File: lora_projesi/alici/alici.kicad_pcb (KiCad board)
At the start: 4 copper layers, 88 x 102 mm, 127 parts, among them J1 USB-C, J2 SMA, J3 RJ45, J4 u.FL (ANA ANTEN), J5 12 V GIRIS, J6 LAMBA, J7 MICRO-SIM, J8 u.FL (YARDIMCI ANTEN, ISTEGE 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, K1 SRD-12VDC-SL-A, Q1 AO3401A, Q2 MMBT2222A, Q3 MMBT2222A, Q4 MMBT2222A, SW1 DUGME, U1 ESP32-S3-WROOM-1-N4, U10 SIM7600SA, U11 AP2112K-3.3, U12 ESDA6V1-5SC6, U4 RFM95W-915S2, U5 TPS62933DRLR, U6 TPS62933DRLR, U7 USBLC6-2SC6, U8 TXB0104PW, U9 W5500, Y1 25 MHz

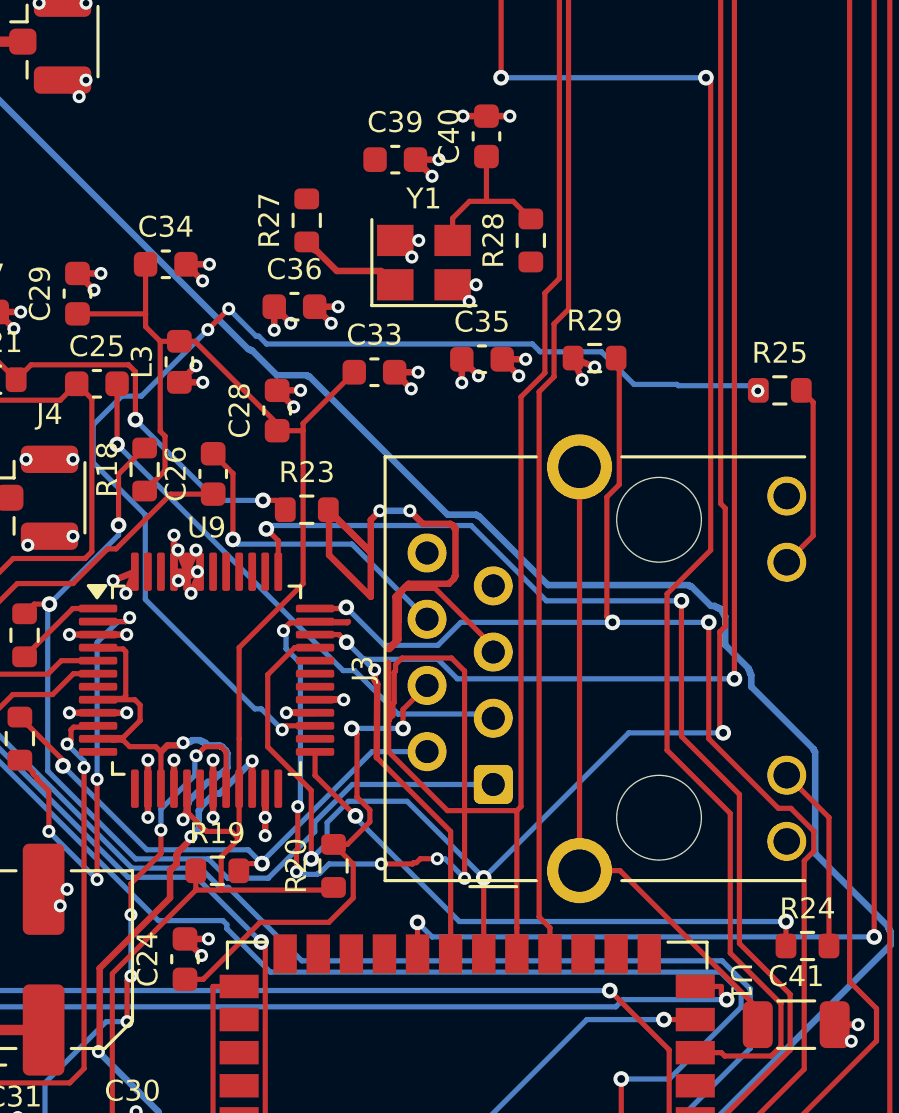
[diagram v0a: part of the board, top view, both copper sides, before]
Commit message: izgara: uc katman (F, B, In2) yonlendirme
Co-Authored-By: Claude Sonnet 5.5 <noreply@anthropic.com>
Claude-Session: https://claude.ai/code/session_01Q71gHQtKJ86ZE2CtYTYSwP
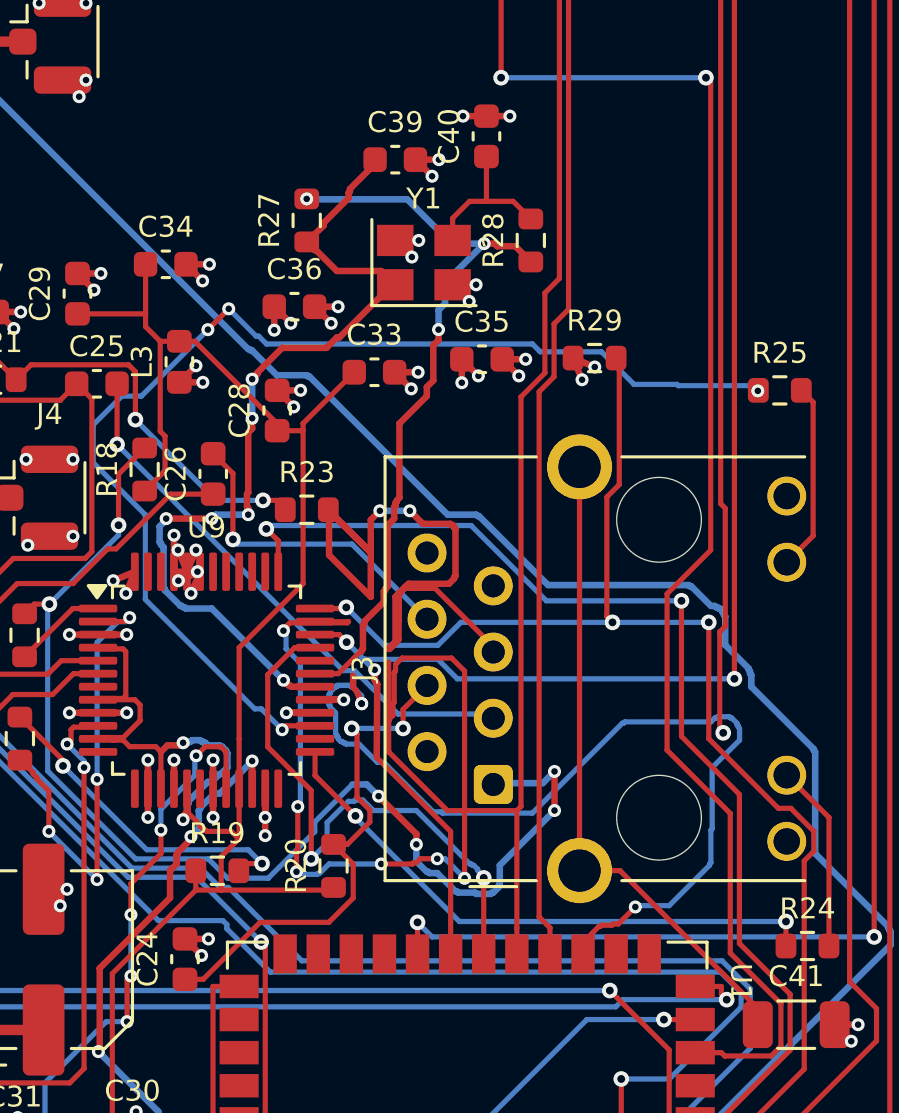
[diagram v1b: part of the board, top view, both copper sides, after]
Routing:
- net ETH_CS: track 0.00 -> 38.3 mm, vias 0 -> 3
- net XI: track 4.08 -> 34.1 mm, vias 0 -> 6
- net XO: track 0.00 -> 29.3 mm, vias 0 -> 3
- net SPI_SCK: track 81.8 -> 70.4 mm, vias 3 -> 4
- net TD_P: track 35.5 -> 46.1 mm, vias 2 -> 7
- net TD_N: track 20.9 -> 12.8 mm

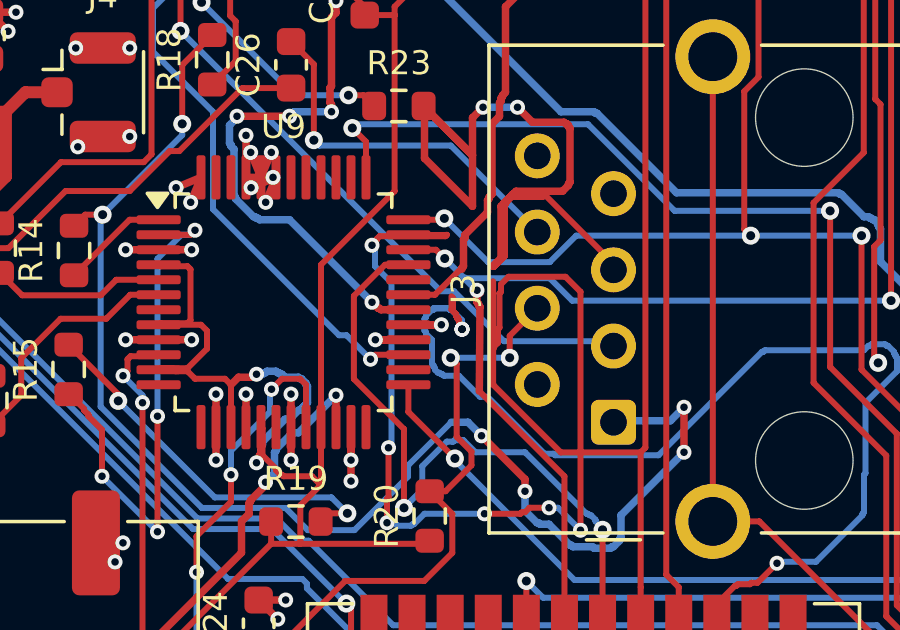
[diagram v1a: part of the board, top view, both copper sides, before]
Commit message: Alici: kristal arka yuz, plane via ic tarafa, boru hatti yeniden
Co-Authored-By: Claude Sonnet 5.5 <noreply@anthropic.com>
Claude-Session: https://claude.ai/code/session_01Q71gHQtKJ86ZE2CtYTYSwP
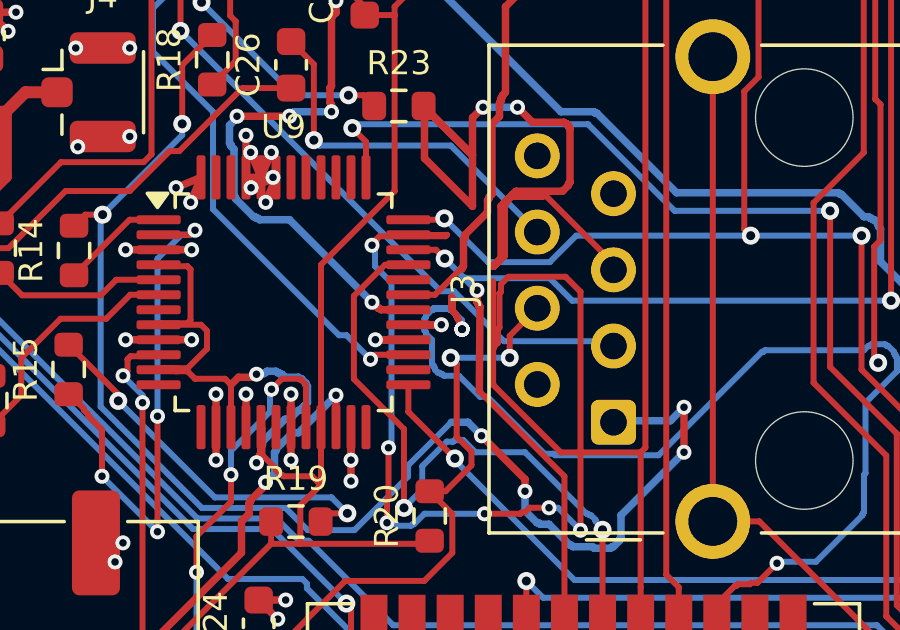
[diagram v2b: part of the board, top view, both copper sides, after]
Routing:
- net ETH_CS: track 38.3 -> 43.6 mm, vias 3 -> 5

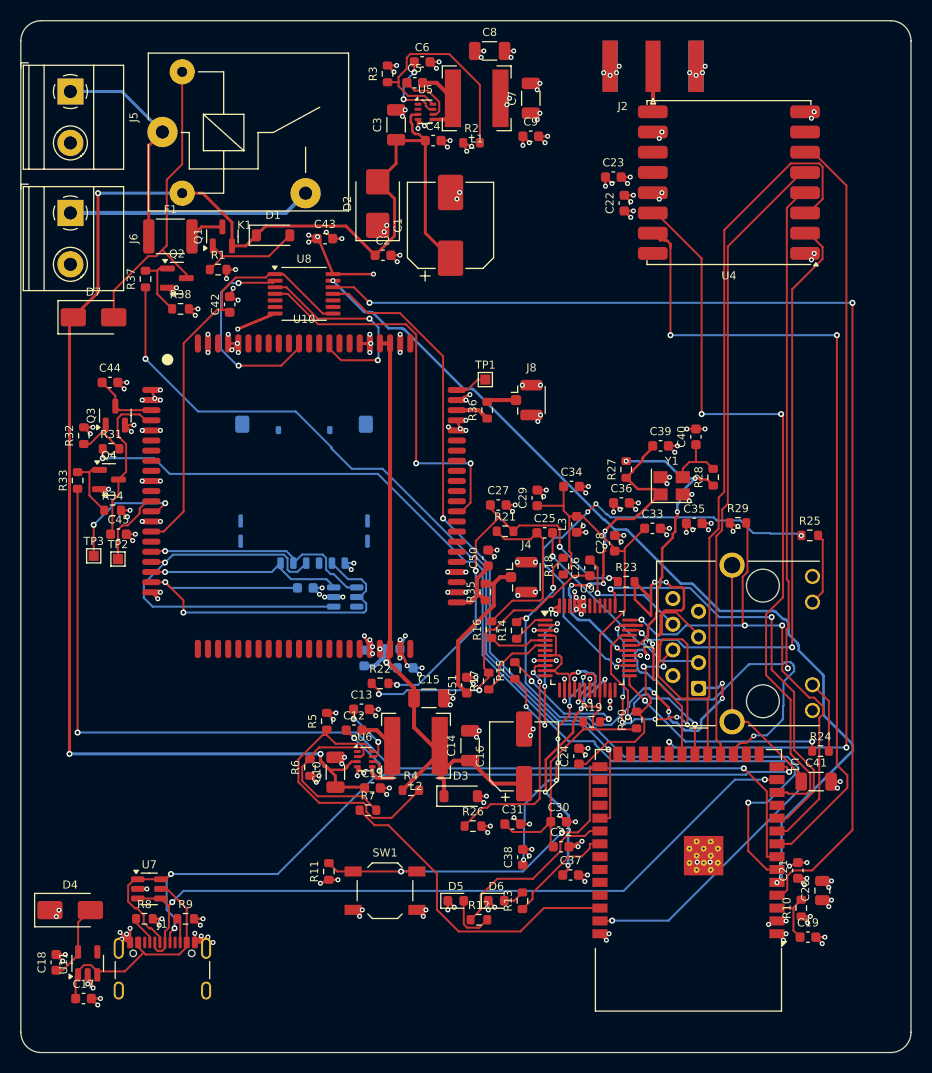
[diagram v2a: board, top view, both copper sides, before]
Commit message: Alici: boru hatti ara hal
Co-Authored-By: Claude Sonnet 5.5 <noreply@anthropic.com>
Claude-Session: https://claude.ai/code/session_01Q71gHQtKJ86ZE2CtYTYSwP
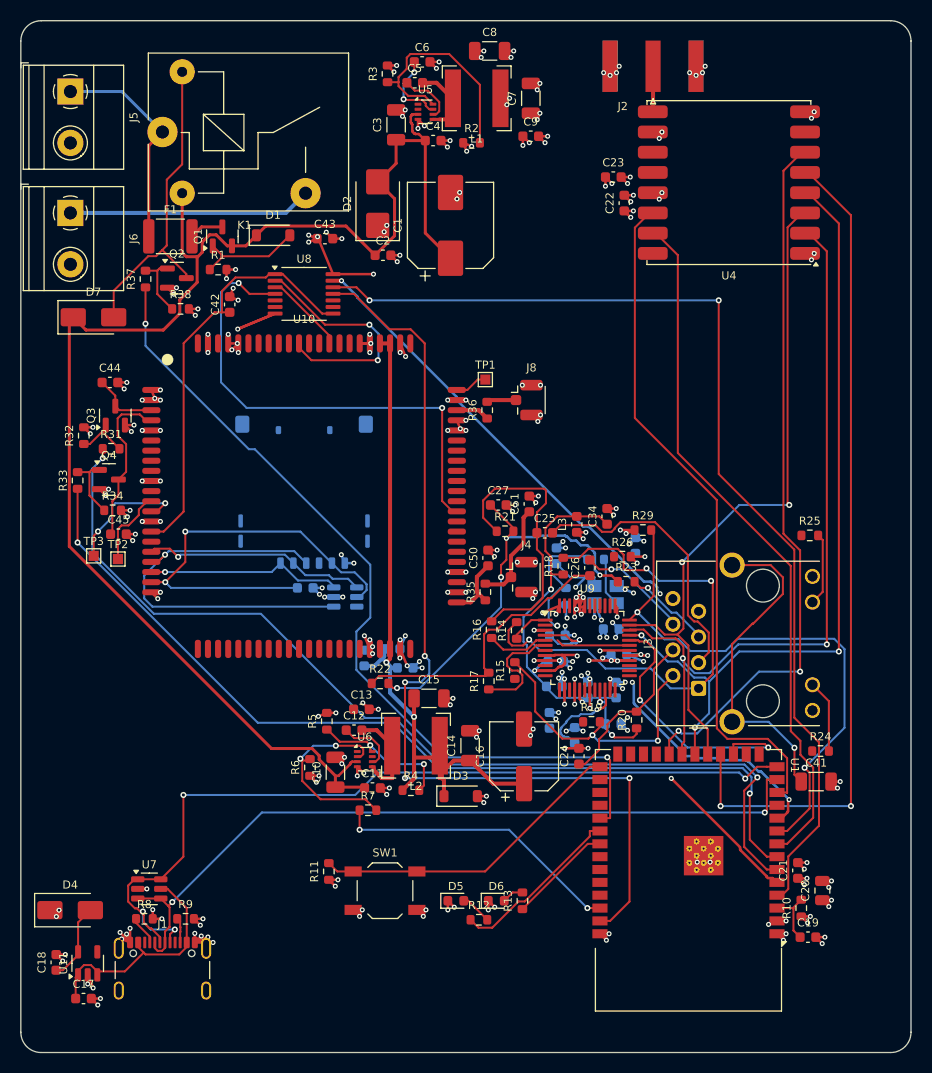
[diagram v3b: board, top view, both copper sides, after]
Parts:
- C28, C29, C30, C31, C32, C33, C35, C36, C37, C38, C39, C40, R27, R28, Y1: moved to B.Cu
- moved R26 30.5 mm to (59.5, 53.0)
- moved C33 19.7 mm to (58.6, 69.5)
- moved C51 19.0 mm to (50.3, 47.8)
- moved C32 16.4 mm to (58.9, 66.2), turned to 90 degrees
- moved C29 16.3 mm to (52.9, 63.4), turned to 0 degrees
- moved C31 15.2 mm to (56.0, 66.2), turned to 90 degrees
- moved C39 15.0 mm to (53.0, 52.9), turned to 90 degrees
- moved C35 14.9 mm to (59.1, 62.6)
- moved R28 14.2 mm to (56.8, 53.3), turned to 0 degrees
- moved R27 13.9 mm to (53.9, 56.9)
- moved C37 13.8 mm to (54.7, 70.7), turned to 90 degrees
- moved C38 13.8 mm to (52.3, 69.2)
- moved C30 13.4 mm to (52.7, 65.8)
- moved Y1 12.6 mm to (57.8, 56.7)
- moved C36 12.5 mm to (58.4, 60.1)
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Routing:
- net SPI_MOSI: track 114.9 -> 68.4 mm, vias 6 -> 2
- net W_ACTLED: track 44.8 -> 0.00 mm, vias 4 -> 0
- net RCT: track 40.3 -> 8.80 mm, vias 2 -> 1
- net +3V3A: track 88.5 -> 63.6 mm, vias 2 -> 8
- net TOCAP: track 24.3 -> 0.00 mm, vias 6 -> 0
- net EXRES1: track 23.0 -> 0.00 mm, vias 2 -> 0
- net W_LINKLED: track 22.3 -> 0.00 mm, vias 2 -> 0
- net LORA_NSS: track 61.5 -> 82.7 mm, vias 0 -> 2
- net W_TXP: track 17.8 -> 0.00 mm, vias 4 -> 0
- net ETH_CS: track 43.6 -> 27.7 mm, vias 5 -> 2
- net TD_N: track 12.8 -> 28.0 mm
- net 1V2O: track 24.2 -> 9.43 mm, vias 4 -> 1
- net XI: track 34.1 -> 19.7 mm, vias 6 -> 3
- net +12V: track 158.9 -> 145.9 mm, vias 3 -> 0
- net LORA_DIO1: track 82.1 -> 69.2 mm, vias 2 -> 0
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
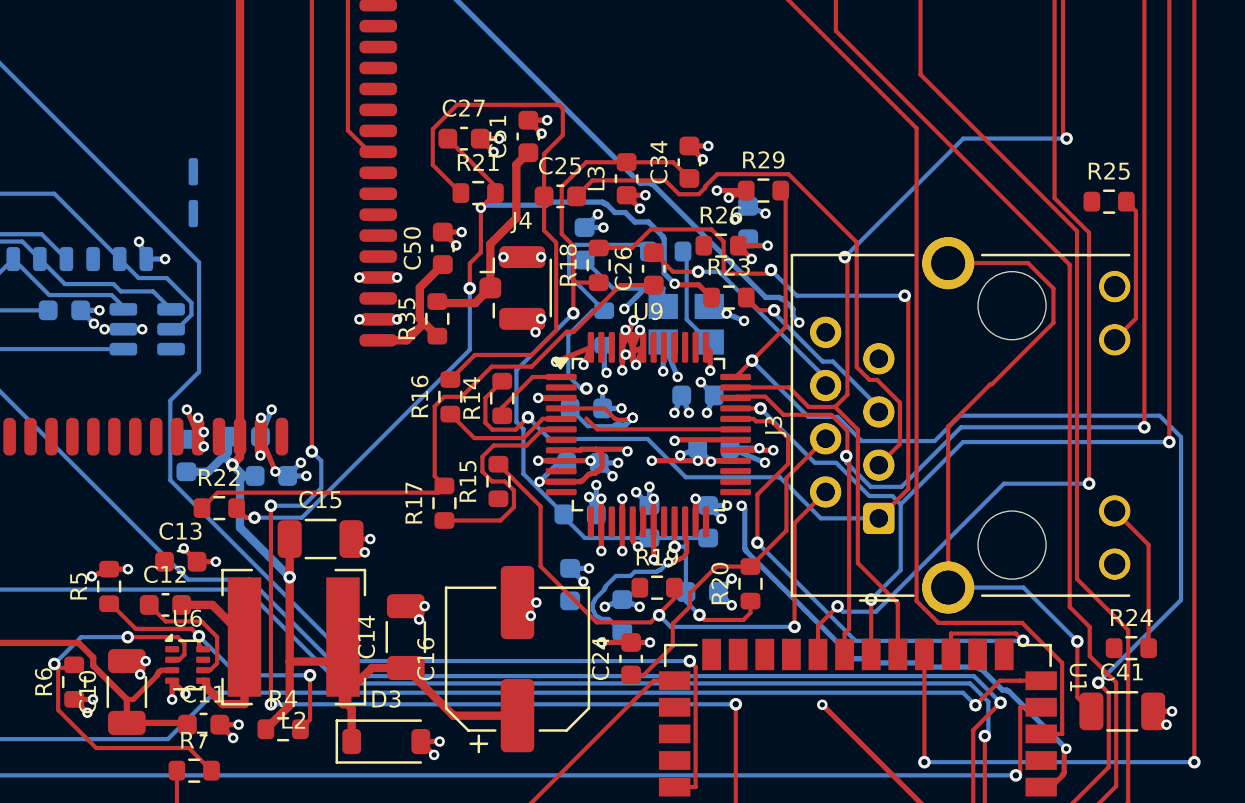
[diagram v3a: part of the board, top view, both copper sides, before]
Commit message: Alici: Freerouting In2 sinyal katmani, boru hatti suruyor
Co-Authored-By: Claude Sonnet 5.5 <noreply@anthropic.com>
Claude-Session: https://claude.ai/code/session_01Q71gHQtKJ86ZE2CtYTYSwP
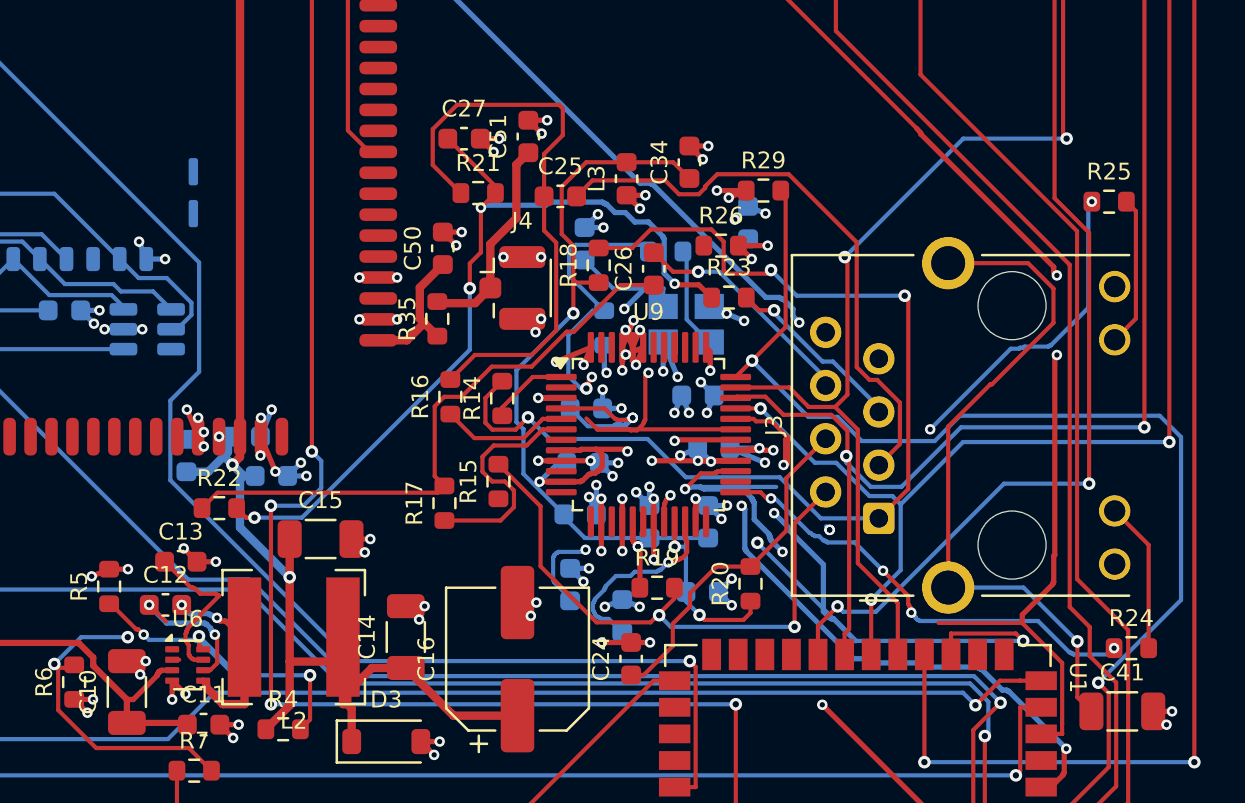
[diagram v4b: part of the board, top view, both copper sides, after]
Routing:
- net W_ACTLED: track 0.00 -> 55.2 mm, vias 0 -> 6
- net W_LINKLED: track 0.00 -> 21.8 mm, vias 0 -> 4
- net XO: track 20.2 -> 34.8 mm, vias 1 -> 3
- net TOCAP: track 0.00 -> 10.8 mm, vias 0 -> 2
- net SS_MOD: track 0.00 -> 7.62 mm
- net ETH_CS: track 27.7 -> 35.0 mm, vias 2 -> 4
- net MODEM_EN: track 19.7 -> 16.0 mm
- net LORA_DIO0: track 67.8 -> 70.8 mm, vias 0 -> 2
- net FB_MOD: track 14.5 -> 17.1 mm, vias 2 -> 3
- net +3V3A: track 63.6 -> 65.6 mm, vias 8 -> 9
- net BST_MOD: track 5.94 -> 7.12 mm, vias 0 -> 2
- net VBAT_MOD: track 71.2 -> 71.6 mm, vias 2 -> 3
- net SW_MOD: vias 0 -> 2
